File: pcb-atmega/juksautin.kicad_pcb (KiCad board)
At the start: 2 copper layers, 65 x 35 mm, 29 parts, among them J1 Screw_Terminal_01x09, J3 USB_C_Receptacle_USB2.0, J4 TagConnect, U1 SP3485EN, U2 SRV05-4, U3 LM2576S-5, U4 ATmega32U4-AU, Y1 X322516MLB4SI

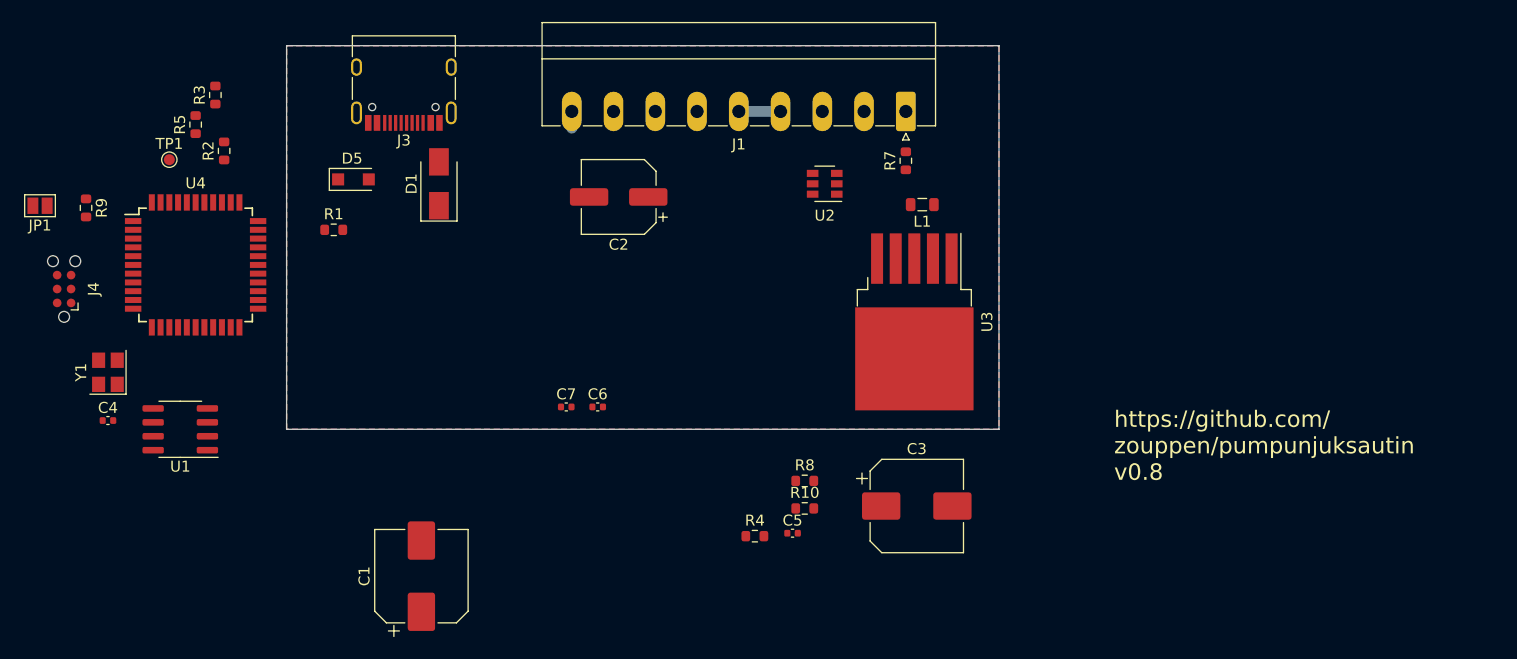
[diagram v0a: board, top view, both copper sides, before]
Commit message: pcb: Route everything Atmega board
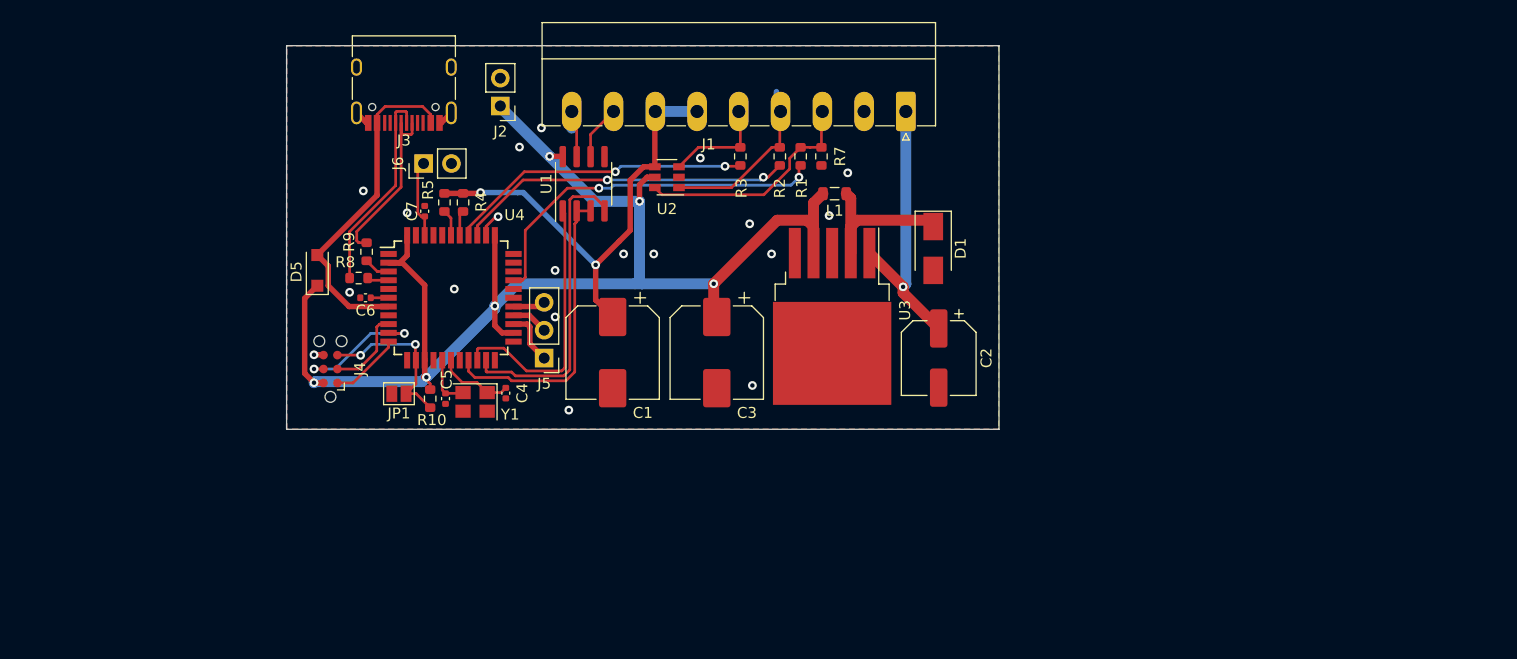
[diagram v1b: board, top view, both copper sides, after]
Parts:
- removed TP1: AR, TestPoint:TestPoint_Pad_D1.0mm
- added J2: Power out, Connector_PinHeader_2.54mm:PinHeader_1x02_P2.54mm_Vertical, F.Cu at (129.5, 70.5)
- added J5: Conn_01x03, Connector_PinHeader_2.54mm:PinHeader_1x03_P2.54mm_Vertical, F.Cu at (133.5, 93.5)
- added J6: AREF_OUT, Connector_PinHeader_2.54mm:PinHeader_1x02_P2.54mm_Vertical, F.Cu at (122.5, 75.8)
- moved R2 50.7 mm to (155.0, 75.1)
- moved R3 48.2 mm to (151.4, 75.1)
- moved D1 45.5 mm to (169.0, 83.5), turned to 270 degrees
- moved R8 44.7 mm to (116.6, 86.2)
- moved R1 43.1 mm to (156.9, 75.1), turned to 90 degrees
- moved U1 43.1 mm to (137.1, 77.6), turned to 90 degrees
- moved R4 40.4 mm to (126.1, 79.3), turned to 90 degrees
- moved JP1 37.0 mm to (120.2, 96.8)
- moved C4 36.4 mm to (130.0, 96.7), turned to 270 degrees
- moved R10 35.6 mm to (123.1, 97.2), turned to 270 degrees
- moved C5 34.0 mm to (124.5, 97.2), turned to 270 degrees
- moved Y1 33.6 mm to (127.2, 97.5), turned to 180 degrees
- moved C2 32.7 mm to (169.5, 93.5), turned to 270 degrees
- moved C1 26.8 mm to (139.8, 93.0), turned to 270 degrees
- moved R9 25.9 mm to (117.3, 83.8)
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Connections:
- C1 pad 1: K5 -> K9
- J1 pad 1: PUMPFAIL -> VIN
- J1 pad 2: IO1 -> GND
- J1 pad 3: IO2 -> PUMPFAIL
- J1 pad 4: K5 -> IO1
- J1 pad 5: K5 -> IO2
- J1 pad 6: A -> K9
- J1 pad 7: B -> K9
- J1 pad 8: VIN -> A
- J1 pad 9: GND -> B
- J3 pad A5: Net-(J3-PadA5) -> (no net)
- J3 pad A8: Net-(J3-PadA8) -> (no net)
- J3 pad B5: Net-(J3-PadB5) -> (no net)
- J3 pad B8: Net-(J3-PadB8) -> (no net)
- R4 pad 2: K5 -> K9
- R5 pad 2: K5 -> K9
- U2 pad 4: PUMPFAIL -> K9
- U2 pad 6: K5 -> PUMPFAIL
- U4 pad 1: Net-(U4-Pad1) -> (no net)
- U4 pad 12: Net-(U4-Pad12) -> (no net)
- U4 pad 18: Net-(U4-Pad18) -> (no net)
- U4 pad 22: Net-(U4-Pad22) -> (no net)
- U4 pad 28: Net-(U4-Pad28) -> (no net)
- U4 pad 29: Net-(U4-Pad29) -> (no net)
- U4 pad 31: Net-(U4-Pad31) -> (no net)
- U4 pad 32: Net-(U4-Pad32) -> (no net)
- U4 pad 33: Net-(U4-Pad33) -> (no net)
- U4 pad 40: Net-(U4-Pad40) -> (no net)
- U4 pad 41: Net-(U4-Pad41) -> (no net)
- U4 pad 8: Net-(U4-Pad8) -> (no net)
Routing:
- net VCC: track 0.00 -> 130.0 mm, vias 0 -> 6
- net K9: track 0.00 -> 42.6 mm, vias 0 -> 2
- net /PUMPFAIL_M: track 0.00 -> 33.6 mm, vias 0 -> 2
- net /VBUS: track 0.00 -> 30.8 mm
- net /IO1_M: track 0.00 -> 30.8 mm, vias 0 -> 2
- net /TX: track 0.00 -> 28.6 mm
- net /IO2_M: track 0.00 -> 27.9 mm, vias 0 -> 2
- net /TX_EN: track 0.00 -> 27.4 mm
- net VIN: track 0.00 -> 25.6 mm, vias 0 -> 1
- net /RX: track 0.00 -> 24.4 mm
- net PUMPFAIL: track 0.00 -> 21.1 mm
- net Net-(J3-PadA6): track 0.00 -> 18.9 mm
- net Net-(J3-PadA7): track 0.00 -> 16.4 mm
- net Net-(D1-Pad1): track 0.00 -> 16.0 mm
- net /RESET: track 0.00 -> 15.2 mm, vias 0 -> 2
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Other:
- board text added: "v0.9 https://github.com/zouppen/pumpunjuksautin"
- board text removed: "https://github.com/ zouppen/pumpunjuksautin v0.8"

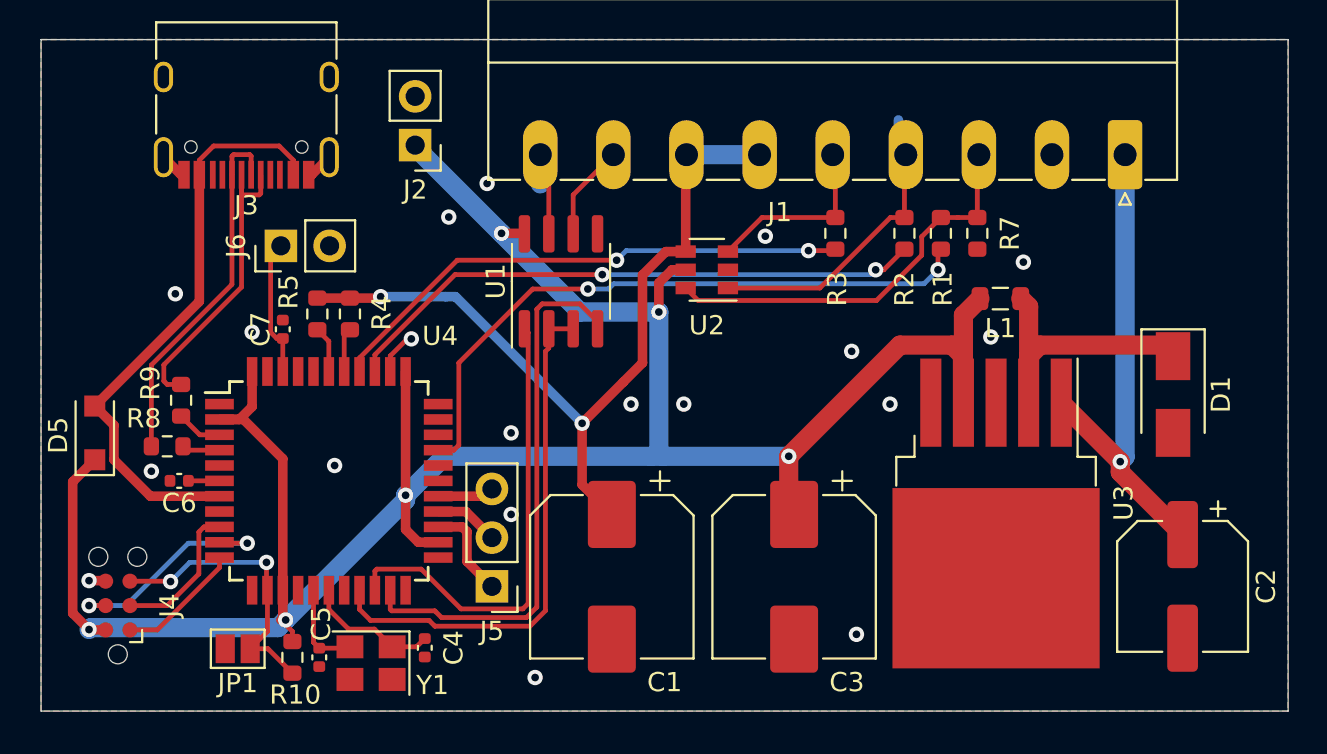
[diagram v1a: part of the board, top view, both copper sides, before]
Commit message: pcb: Rerouting and cleanup
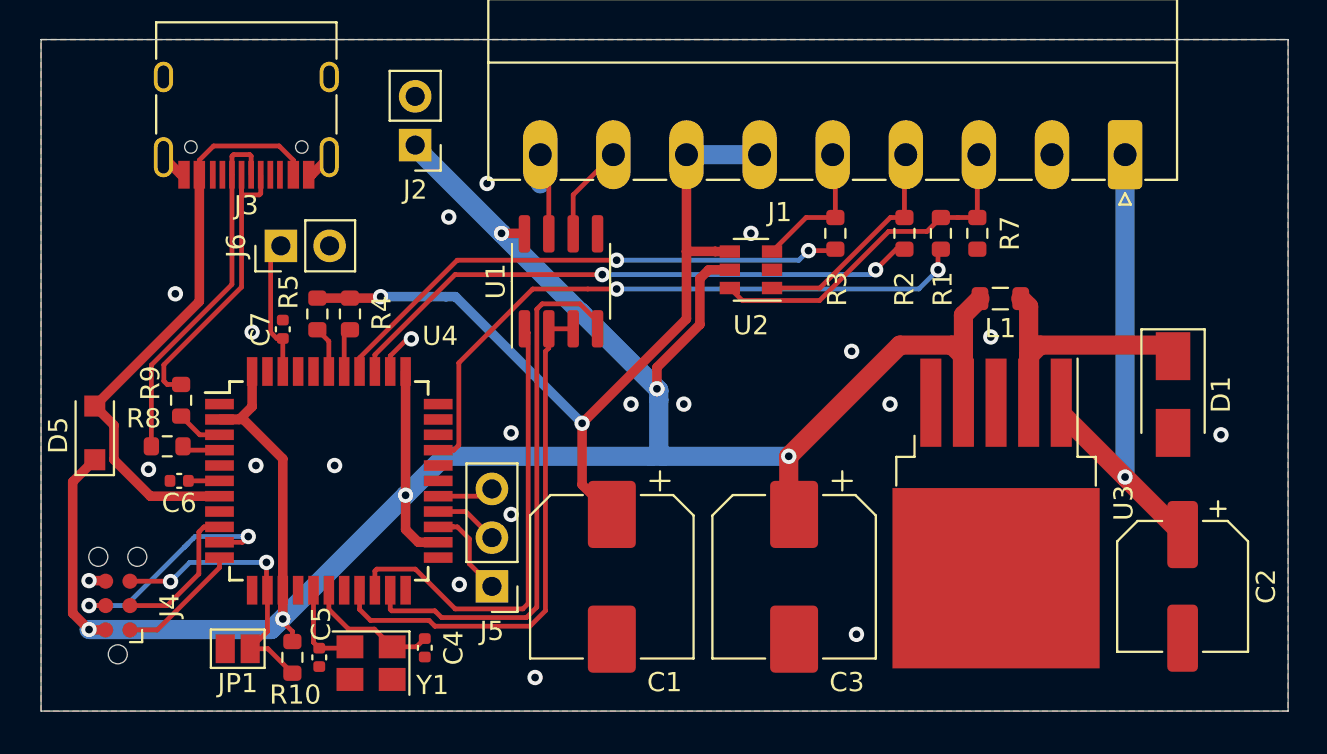
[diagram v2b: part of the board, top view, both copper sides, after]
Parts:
- J5: value Conn_01x03 -> EXTRA
- moved U2 2.30 mm to (147.0, 77.0)
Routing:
- net IO1: track 16.8 -> 11.7 mm
- net VCC: track 130.0 -> 133.2 mm
- net PUMPFAIL: track 21.1 -> 18.3 mm
- net IO2: track 9.67 -> 7.37 mm
- net K9: track 42.6 -> 44.3 mm
- net /MOSI: track 11.9 -> 12.7 mm
- net VIN: track 25.6 -> 26.3 mm
- net GND: track 6.05 -> 6.15 mm, vias 19 -> 21
